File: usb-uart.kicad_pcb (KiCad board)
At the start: 2 copper layers, 43.5 x 28.5 mm, 21 parts, among them CN1 USB4110-GF-A, CN2 30310-5002HB, SW1 CUS-12B, U1 PRTR5V0U2X, U2 FT231XQ

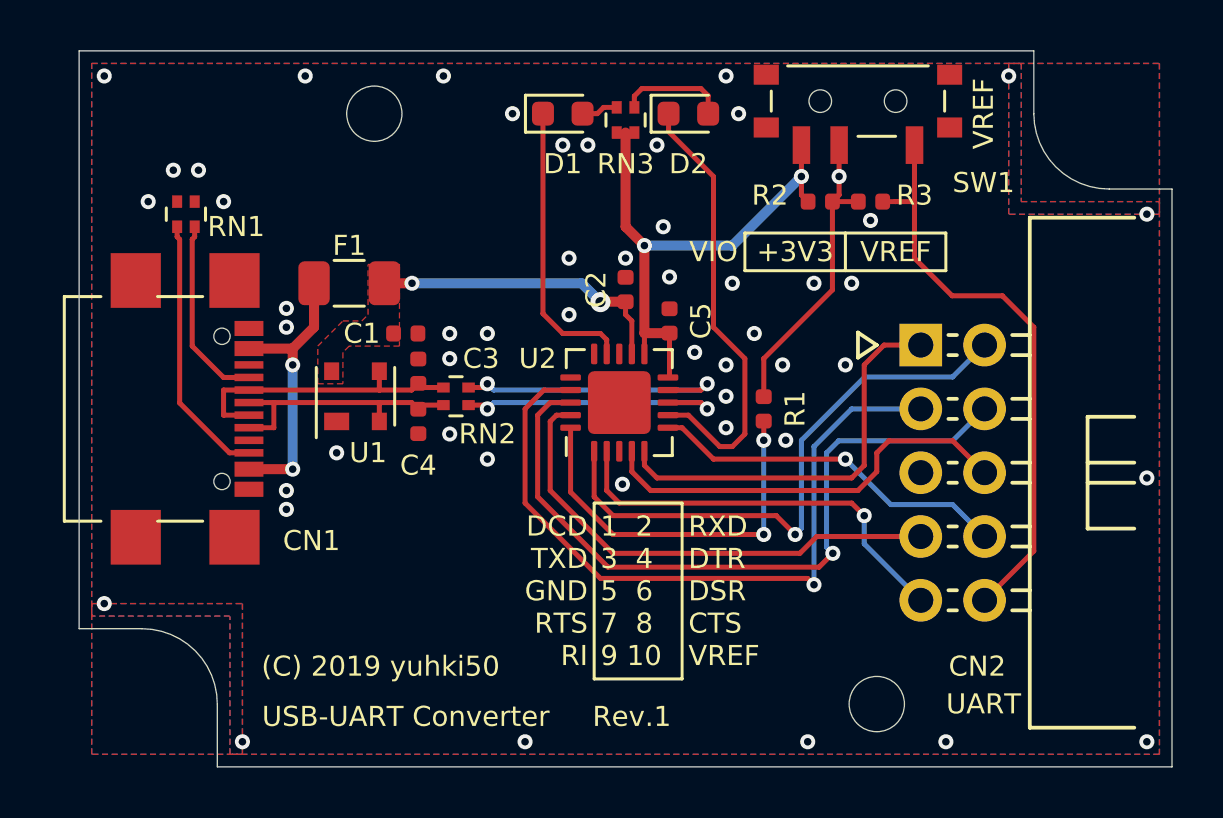
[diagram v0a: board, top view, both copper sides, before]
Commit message: Update
* USB Type Cのプルアップ抵抗のフットプリントを変更する
* USB Type Cをより基板から飛び出す
* R4を未実装にする
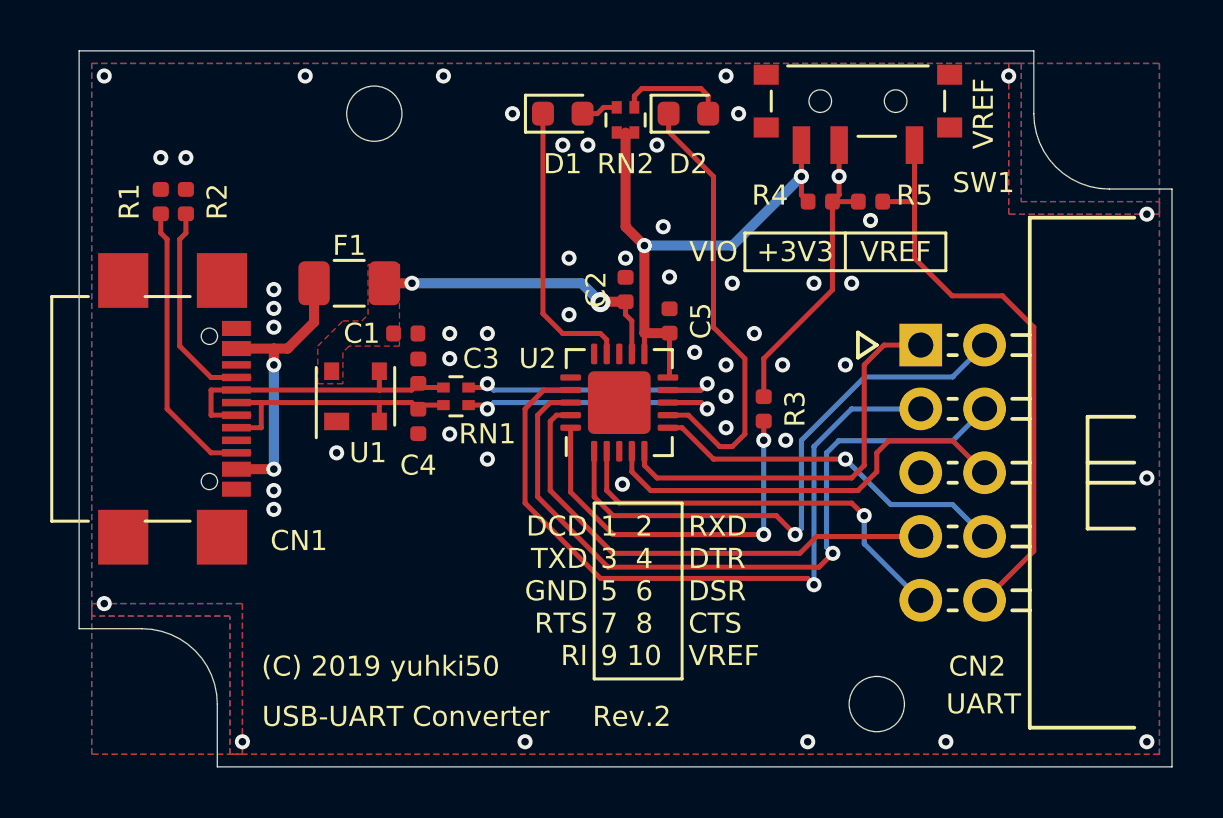
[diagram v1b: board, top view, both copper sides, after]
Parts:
- removed the RN1 at (114.2, 76.5)
- added R1: 5.1k, Resistor_SMD:R_0402_1005Metric, F.Cu at (113.2, 76.0)
- added R2: 5.1k, Resistor_SMD:R_0402_1005Metric, F.Cu at (114.2, 76.0)
- R4: renamed from R2; value 0 -> DNP
- moved CN1 0.50 mm to (113.8, 84.2)
- renumbered R1 to R3, R3 to R5, RN2 to RN1, RN3 to RN2
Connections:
- CN1 pad A8: (no net) -> Net-(CN1-PadA8)
- CN1 pad B8: (no net) -> Net-(CN1-PadB8)
- U2 pad 15: (no net) -> Net-(U2-Pad15)
- U2 pad 16: (no net) -> Net-(U2-Pad16)
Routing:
- net Net-(CN1-PadB5): track 10.6 -> 11.9 mm
- net Net-(CN1-PadA5): track 7.57 -> 8.65 mm
- net Net-(C3-Pad1): track 11.7 -> 12.7 mm
- net GND: vias 50 -> 49
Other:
- board text added: "Rev.2"
- board text removed: "Rev.1"
